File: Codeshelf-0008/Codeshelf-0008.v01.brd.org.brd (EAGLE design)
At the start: 140.1 x 99 mm, 53 parts, among them J1 M05X2PTH, J2 RJ45-8PTH, J3-WAKE M02PTH, J4 RJ45-8PTH, J5 HEADER-2X-2.54MM, U1 ZSFM201-1A, U2 MAX232SOIC16, U3 RS485SOIC, U4 ULN2003AD, U5 MIC94061C6, U6 MIC94061C6

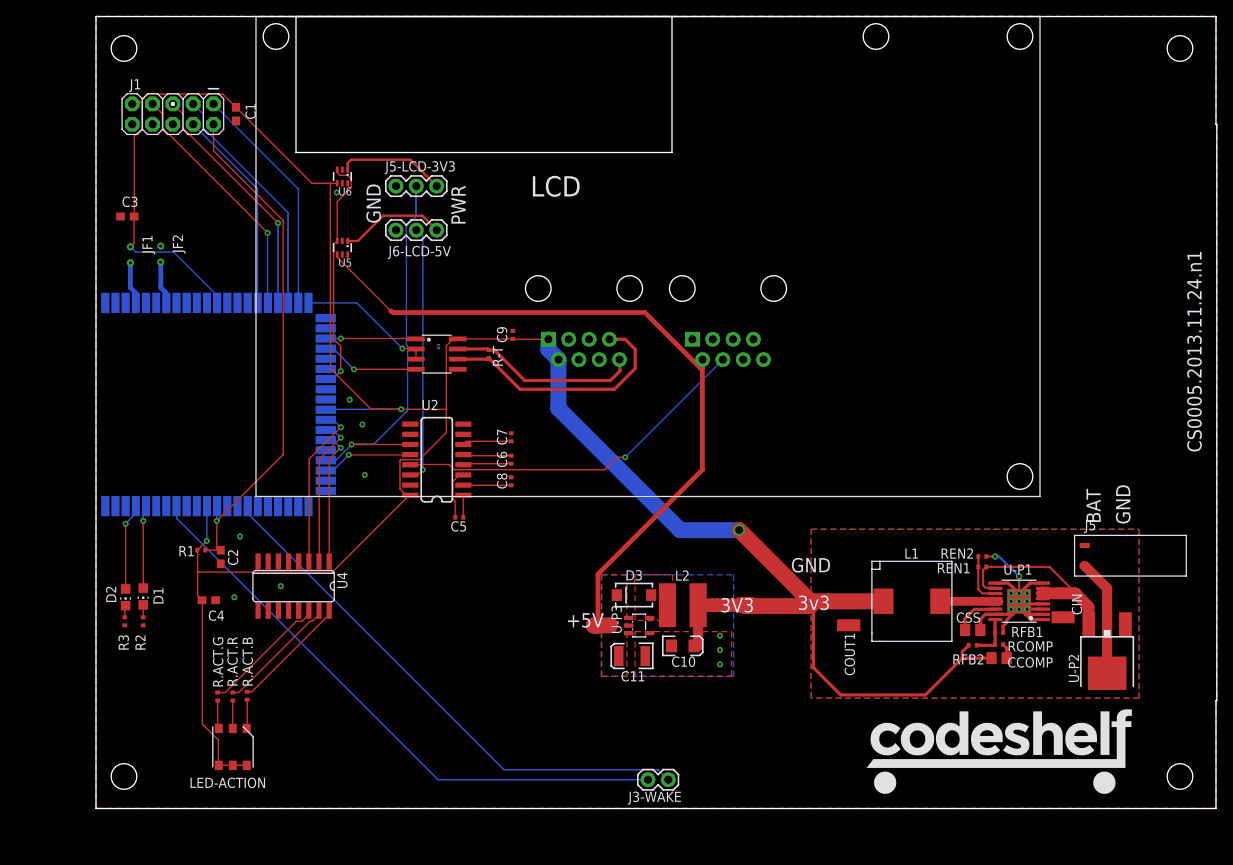
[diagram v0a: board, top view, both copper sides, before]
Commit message: New position controller design
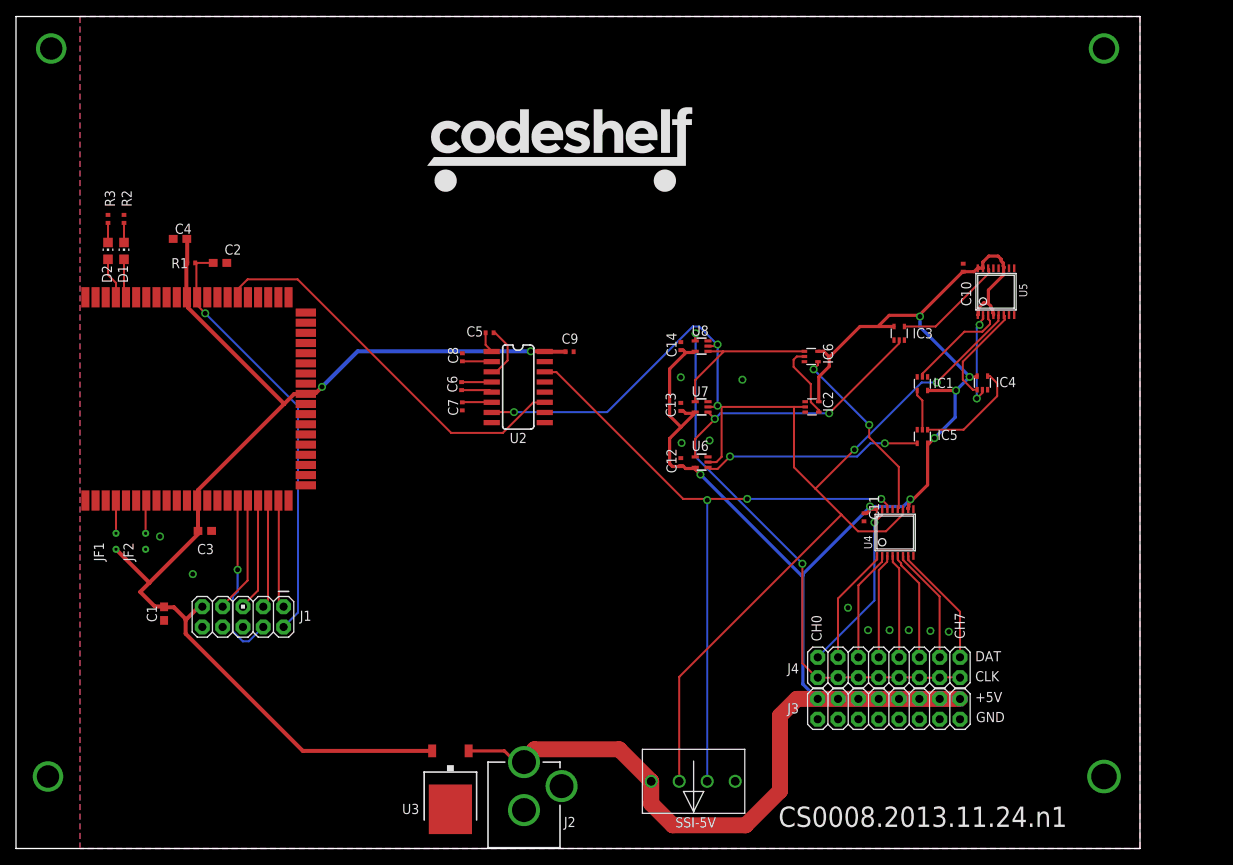
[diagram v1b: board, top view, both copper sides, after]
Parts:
- removed CCOMP: 68pF, GW-devices:C0805
- removed CIN: 47uF, GW-devices:C1210K
- removed COUT1: 100uF, GW-devices:C1210K
- removed CSS: 2.7nF, GW-devices:C0805
- removed D3: MBRA140, SparkFun:SMA-DIODE
- removed J3-WAKE: M02PTH, SparkFun-Connectors:1X02
- removed J5: HEADER-2X-2.54MM, GW-devices:HEADER-2X-RA-2.54MM
- removed J5-LCD-3V3, J6-LCD-5V: (no value), SparkFun-Connectors:1X03
- removed L1: 150uH, GW-devices:SLF10165
- removed L2: 47uH, SparkFun:CR54
- removed LCD: LCD-SPARKFUN, GW-devices:LCD-20X4-SPARKFUN
- removed LED-ACTION: LED5060A, GW-devices:PLCC-6
- removed LOGO: CODESHELF-LOGO, GW-devices:CODESHELF-LOGO
- removed R-T: 120, GW-devices:RF-R0402
- removed R.ACT.B, R.ACT.G: 10, GW-devices:RF-R0402
- removed R.ACT.R: 68, GW-devices:RF-R0402
- removed RCOMP: 4.64K, GW-devices:RF-R0402
- removed REN1: 22K, GW-devices:RF-R0402
- removed REN2: 10K, GW-devices:RF-R0402
- removed RFB1: 45.3K, GW-devices:RF-R0402
- removed RFB2: 143K, GW-devices:RF-R0402
- removed U-P1: LM2854MH, GW-devices:HTSSOP16PWP
- removed U-P2: PCHANNEL-MOSFET-DPAK, GW-devices:DPAK
- removed U-P3: NCP1402, SparkFun:SOT23-5
- added C12, C13, C14: .1uF, GW-devices:C0402
- added IC1, IC2, IC3: 74AHC1G04DCK, 74xx-little-us:SC70-5
- added IC4, IC5, IC6: 74AHC1G08DCK, 74xx-little-us:SC70-5
- added J3: M08X2, SparkFun:2X8
- added SSI-5V: HEADER-4X39357, GW-devices:MOLEX-39357-0004
- added U$1: (no value), GW-devices:CODESHELF-LOGO
- added U7, U8: D-FLIP-FLOP-74LV1G79, GW-devices:SOT353
- C10: value 10uF -> .1uF; device SparkFun:EIA3216 -> GW-devices:C0402
- C11: value 68uF -> .1uF; device SparkFun:EIA3528 -> GW-devices:C0402
- J2: value RJ45-8PTH -> POWER_JACKPTH; device SparkFun:RJ45-8 -> GW-devices:POWER_JACK_PTH
- J4: value RJ45-8PTH -> M08X2; device SparkFun:RJ45-8 -> SparkFun:2X8
- U3: value RS485SOIC -> LM2936DT-3.3; device SparkFun:SO08 -> national-semiconductor:TO252
- U4: value ULN2003AD -> SN74HC595PW; device uln-udn:SO16 -> GW-devices:TSSOP16
- U5: value MIC94061C6 -> 74HCT193PW; device GW-devices:SC70-6L -> GW-devices:TSSOP16
- U6: value MIC94061C6 -> D-FLIP-FLOP-74LV1G79; device GW-devices:SC70-6L -> GW-devices:SOT353
- moved U5 81.9 mm to (122.5, 69.6), turned to 0 degrees
- moved J2 77.2 mm to (63.5, -2.90), flipped to the top, turned to 0 degrees
- moved U4 75.5 mm to (109.9, 39.5), turned to 0 degrees
- moved J4 65.8 mm to (118.0, 23.9), flipped to the top
- moved J1 63.4 mm to (28.4, 29.0)
- moved C1 63.1 mm to (18.5, 29.4)
- moved C10 58.8 mm to (118.4, 72.6), turned to 90 degrees
- moved U6 57.4 mm to (85.7, 48.3), turned to 90 degrees
- moved U3 54.4 mm to (54.3, 7.40), turned to 180 degrees
- moved R2 50.4 mm to (13.5, 78.7), turned to 270 degrees
- moved R3 50.3 mm to (11.5, 78.7), turned to 270 degrees
- moved C4 45.3 mm to (20.5, 76.2), turned to 0 degrees
- moved D2 43.4 mm to (11.5, 74.7), turned to 0 degrees
- moved D1 43.3 mm to (13.5, 74.7), turned to 0 degrees
- moved C3 40.5 mm to (23.6, 39.7), turned to 180 degrees
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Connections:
- removed net N$21: J4.7, R-T.2, U3.6
- removed net N$34: LED-ACTION.2, R.ACT.R.1
- removed net N$35: LED-ACTION.3, R.ACT.G.1
- removed net N$36: U1.34, U4.1
- removed net N$37: U1.33, U4.2
- removed net N$38: R.ACT.B.2, U4.16
- removed net N$39: U1.32, U4.3
- removed net N$5: D3.A, L2.P$2, U-P3.5
- removed net N$9: U1.28, U5.3, U6.3
- removed net R1IN: J2.4, U2.13
- removed net R1OUT: U1.37, U2.12
- removed net T1IN: J5-LCD-3V3.2, U1.36, U2.11
- removed net T1OUT: J6-LCD-5V.2, U2.14
- removed net V-PROT: CIN.1, REN1.2, U-P1.10, U-P1.5, U-P1.6, U-P1.7, U-P2.3
- removed net VBATT: J5.2, U-P2.4
- new net N$29: IC1.2, U5.3
- new net N$31: IC4.1, U5.6
- new net N$32: IC3.4, U5.14
- new net SSI-CLK: J4.10, J4.12, J4.14, J4.16, J4.2, J4.4, J4.6, J4.8, U8.4
- new net SSI-CLK-3V3: U1.42
- new net SSI-CLK-5V: IC2.2, SSI-5V.3, U2.7, U4.11, U5.5, U6.2, U7.2, U8.2
- new net SSI-TX-3V3: U1.45, U2.11
- new net SSI-TX-5V: SSI-5V.2, U2.14, U4.14
- net +3V3: now also U3.2; no longer C10.A, CCOMP.2, COUT1.1, J4.1, J4.2, L1.2, L2.P$1, LED-ACTION.4, LED-ACTION.5, LED-ACTION.6, RFB2.2, U3.8, U6.4
- net +5V: now also C10.1, C11.2, C12.2, C13.2, C14.2, IC1.5, IC2.5, IC3.5, IC4.5, IC5.5, IC6.5, J2.PWR, J3.1, J3.11, J3.13, J3.15, J3.3, J3.5, J3.7, J3.9, SSI-5V.4, U3.1, U4.10, U4.16, U5.1, U5.11, U5.15, U5.16, U6.5, U7.5, U8.5; no longer C11.A, D3.C, J2.2, U-P3.1, U-P3.2
- net GND: now also C10.2, C11.1, C12.1, C13.1, C14.1, IC1.3, IC2.3, IC3.3, IC4.3, IC5.3, IC6.3, J2.GND, J2.GNDBREAK, J3.10, J3.12, J3.14, J3.16, J3.2, J3.4, J3.6, J3.8, SSI-5V.1, U3.3, U4.13, U5.8, U6.3, U7.3, U8.3; no longer C10.C, C11.C, CIN.2, COUT1.2, CSS.2, J2.3, J4.3, J4.6, J5-LCD-3V3.1, J5.1, J6-LCD-5V.1, REN2.1, RFB1.1, U-P1.1, U-P1.15, U-P1.2, U-P1.3, U-P1.4, U-P1.8, U-P1.9, U-P1.EXP, U-P2.1, U-P3.4, U3.5, U5.2, U5.5, U6.2, U6.5
- net N$10: now also J4.13, U4.1; no longer J5-LCD-3V3.3, U6.1
- net N$13: now also J4.11, U4.2; no longer J6-LCD-5V.3, U5.1
- net N$14: now also J4.9, U4.3; no longer J3-WAKE.2, U1.46
- net N$16: now also J4.7, U4.4; no longer J3-WAKE.1, U1.53
- net N$17: now also J4.5, U4.5; no longer U1.25, U3.4
- net N$18: now also J4.3, U4.6; no longer U1.24, U3.1
- net N$19: now also J4.1, U4.7; no longer U1.21, U3.2, U3.3
- net N$20: now also J4.15, U4.15; no longer J4.8, R-T.1, U3.7
- net N$22: now also IC1.4, IC5.2; no longer CSS.1, U-P1.14
- net N$23: now also IC4.4, IC5.1; no longer L1.1, U-P1.12, U-P1.13
- net N$24: now also IC5.4, U6.1; no longer RCOMP.2, RFB1.2, RFB2.1, U-P1.16
- net N$25: now also IC3.2, U6.4, U7.1; no longer CCOMP.1, RCOMP.1
- net N$26: now also IC6.1, U7.4, U8.1; no longer REN1.1, REN2.2, U-P1.11
- net N$28: now also IC2.4, IC6.2; no longer R.ACT.R.2, U4.15
- net N$30: now also IC4.2, U5.2; no longer R.ACT.G.2, U4.14
- net N$33: now also IC6.4, U4.12; no longer LED-ACTION.1, R.ACT.B.1
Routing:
- net +3V3: track 349.7 -> 149.2 mm, vias 3 -> 2
- net SSI-CLK-5V: track 0.00 -> 163.1 mm, vias 0 -> 5
- net +5V: track 93.0 -> 244.0 mm, vias 0 -> 7
- net SSI-TX-5V: track 0.00 -> 85.6 mm, vias 0 -> 3
- net SSI-CLK: track 0.00 -> 68.4 mm, vias 0 -> 2
- net N$16: track 74.0 -> 13.0 mm
- net N$14: track 67.3 -> 13.1 mm
- net SSI-TX-3V3: track 0.00 -> 49.5 mm
- net T1IN: track 48.8 -> 0.00 mm, vias 1 -> 0
- net GND: track 45.5 -> 0.00 mm, vias 21 -> 12
- net R1IN: track 45.1 -> 0.00 mm, vias 1 -> 0
- net N$25: track 1.89 -> 34.3 mm, vias 0 -> 2
- net T1OUT: track 32.1 -> 0.00 mm, vias 1 -> 0
- net N$21: track 31.1 -> 0.00 mm, vias 0 -> 1
- net N$9: track 30.0 -> 0.00 mm
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- removed copper zone on layer 1, net +5V
- removed copper zone on layer 1, net N$5
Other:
- board size 140.1 x 99 mm -> 140.5 x 104 mm
- board text added: "CH0"
- board text added: "CH7"
- board text added: "CLK"
- board text added: "CS0008.2013.11.24.n1"
- board text added: "DAT"
- board text removed: "3V3"
- board text removed: "3v3"
- board text removed: "BAT"
- board text removed: "CS0005.2013.11.24.n1"
- board text removed: "PWR"
